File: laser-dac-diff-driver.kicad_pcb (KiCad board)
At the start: 2 copper layers, 53 parts, among them IC401 DCDC-CONV_TRACO_TMH-XXXX_Dual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, P101 CONN_2, P102 CONN_3X2, P103 CONN_6X2, U101 AD5689RARUZ, U102 74HC04, U201 OP470, U202 LM358, U401 LM317EMP, U402 LM317EMP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

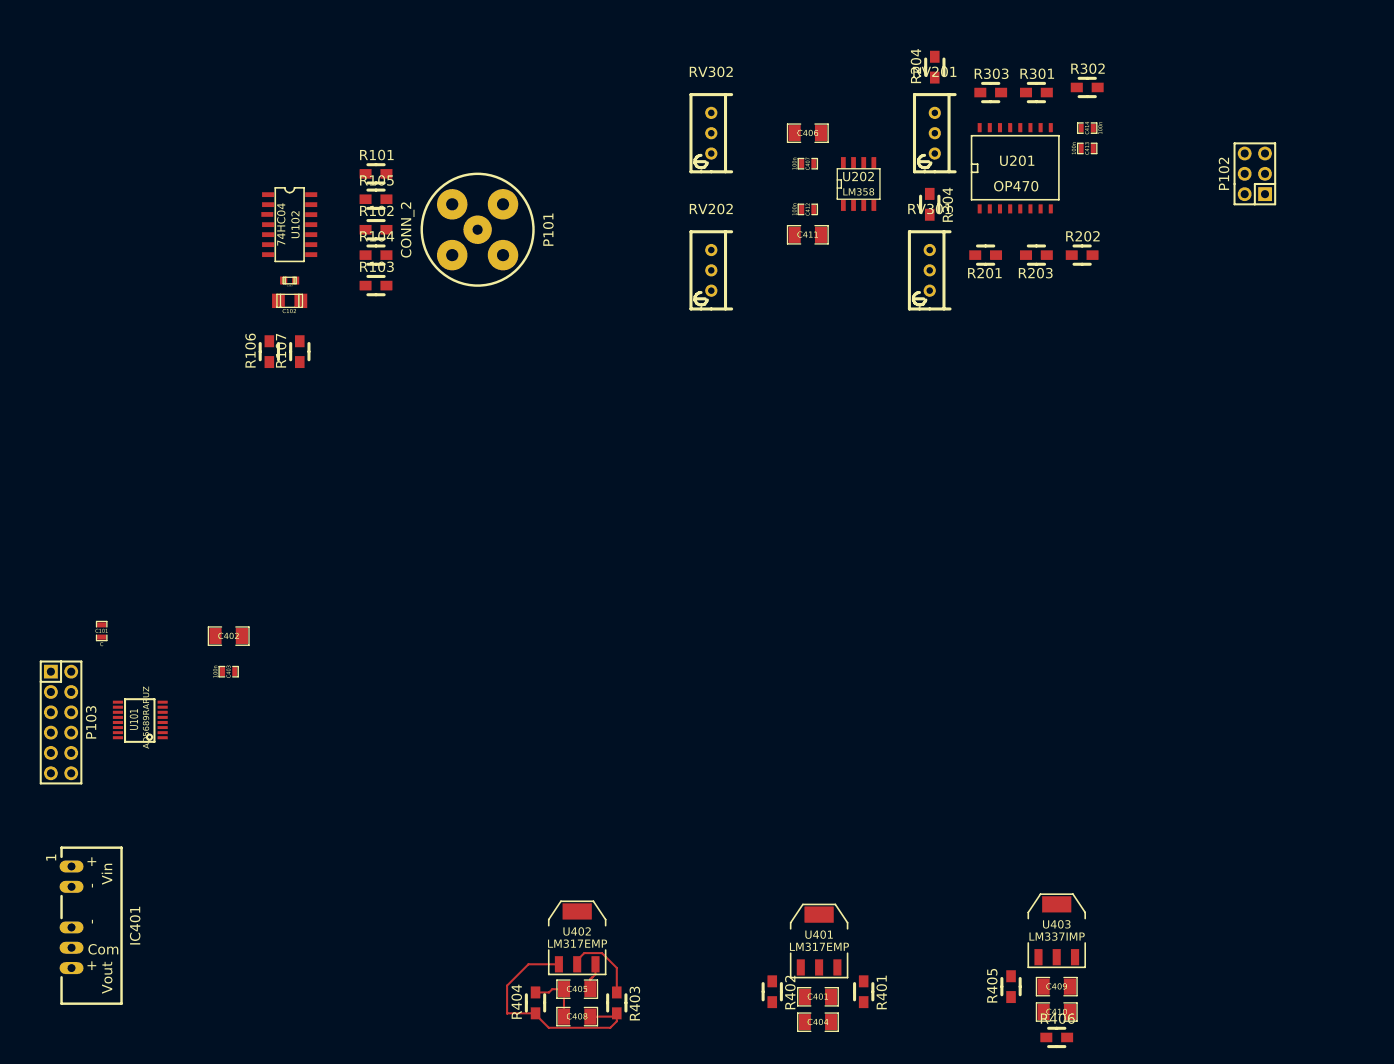
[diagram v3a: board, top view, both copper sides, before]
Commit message: Started layout, final-ish positions
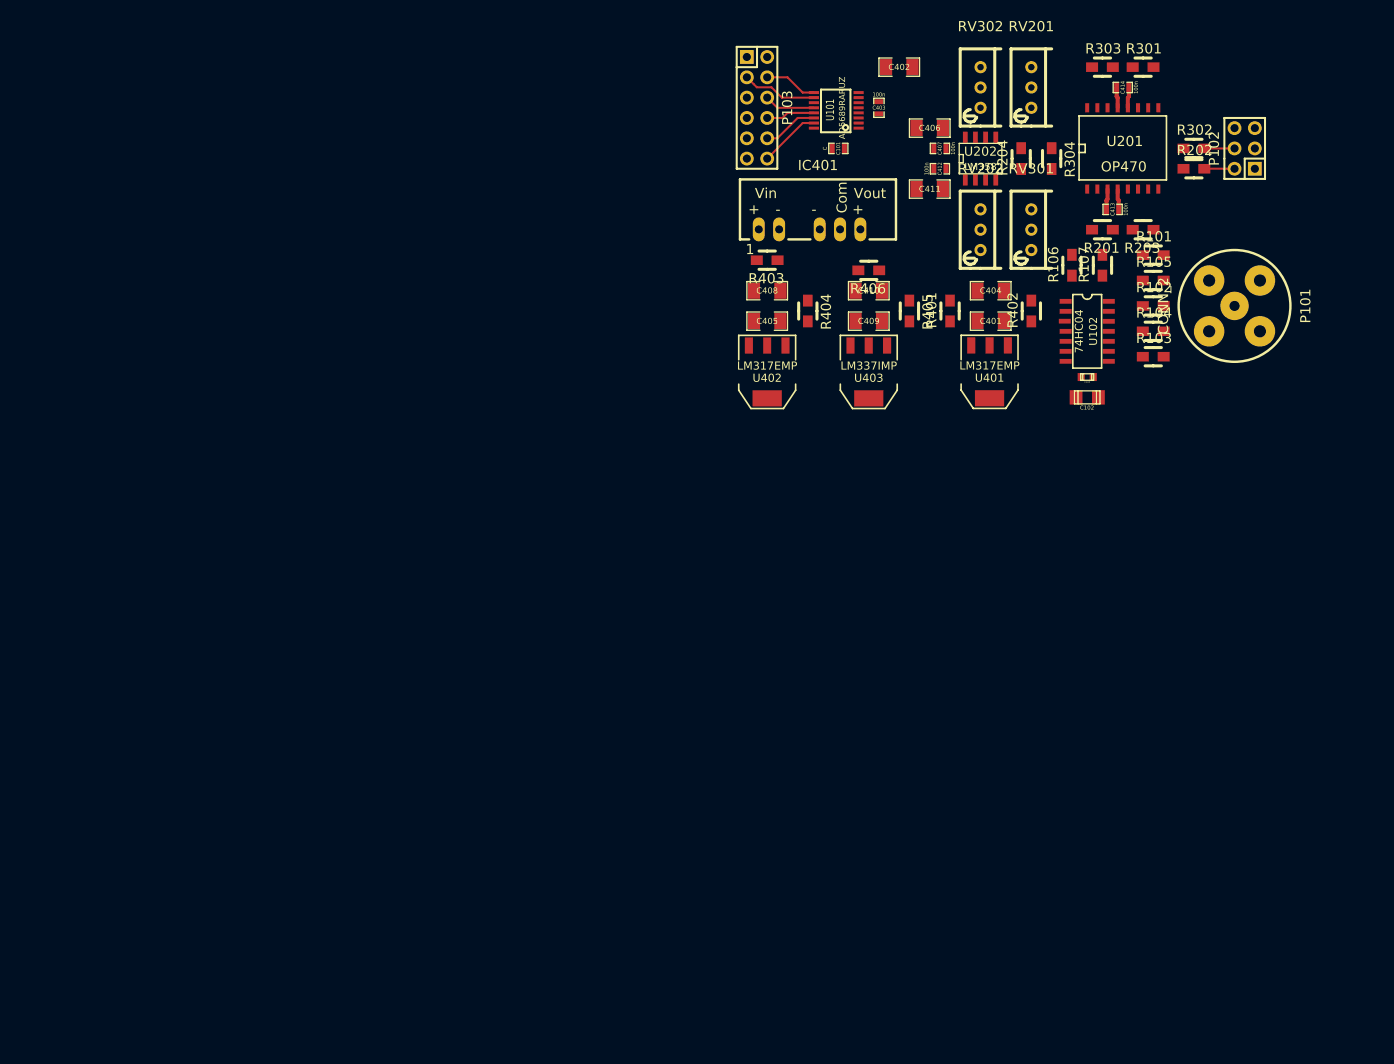
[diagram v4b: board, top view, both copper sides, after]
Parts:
- moved IC401 127.5 mm to (218.4, 44.5), turned to 0 degrees
- moved P103 116.1 mm to (210.8, 31.8)
- moved U101 115.6 mm to (223.5, 34.3)
- moved C101 110.1 mm to (221.0, 36.8), turned to 0 degrees
- moved C402 109.9 mm to (228.6, 26.7)
- moved C403 107.6 mm to (226.1, 31.8), turned to 270 degrees
- moved R107 100.9 mm to (254.0, 51.4)
- moved R106 100.9 mm to (250.2, 51.4)
- moved U102 100.6 mm to (252.1, 59.7)
- moved C103 100.4 mm to (252.1, 65.4)
- moved C102 100.4 mm to (252.1, 67.9)
- moved R406 98.7 mm to (224.8, 52.1), turned to 180 degrees
- moved R101 97.7 mm to (260.4, 50.2)
- moved R105 97.7 mm to (260.4, 53.3)
- moved R102 97.6 mm to (260.4, 56.5)
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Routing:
- net Net-(C408-Pad1): track 30.5 -> 0.00 mm
- net /GAIN: track 0.00 -> 9.43 mm
- net /~RESET: track 0.00 -> 7.68 mm
- net VAA: track 9.67 -> 2.59 mm
- net /SDIN: track 0.00 -> 6.89 mm
- net /~LDAC: track 0.00 -> 6.63 mm
- net /SCLK: track 0.00 -> 6.37 mm
- net /~SYNC: track 0.00 -> 6.11 mm
- net /analog2/Out1+: track 0.00 -> 3.78 mm
- net /analog/Out1+: track 0.00 -> 3.78 mm
- net Net-(C401-Pad1): track 3.41 -> 0.00 mm
- net -VAA: track 0.00 -> 2.59 mm
- net DGND: track 7.16 -> 5.19 mm
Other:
- net class Signal removed
- net class asdf removed

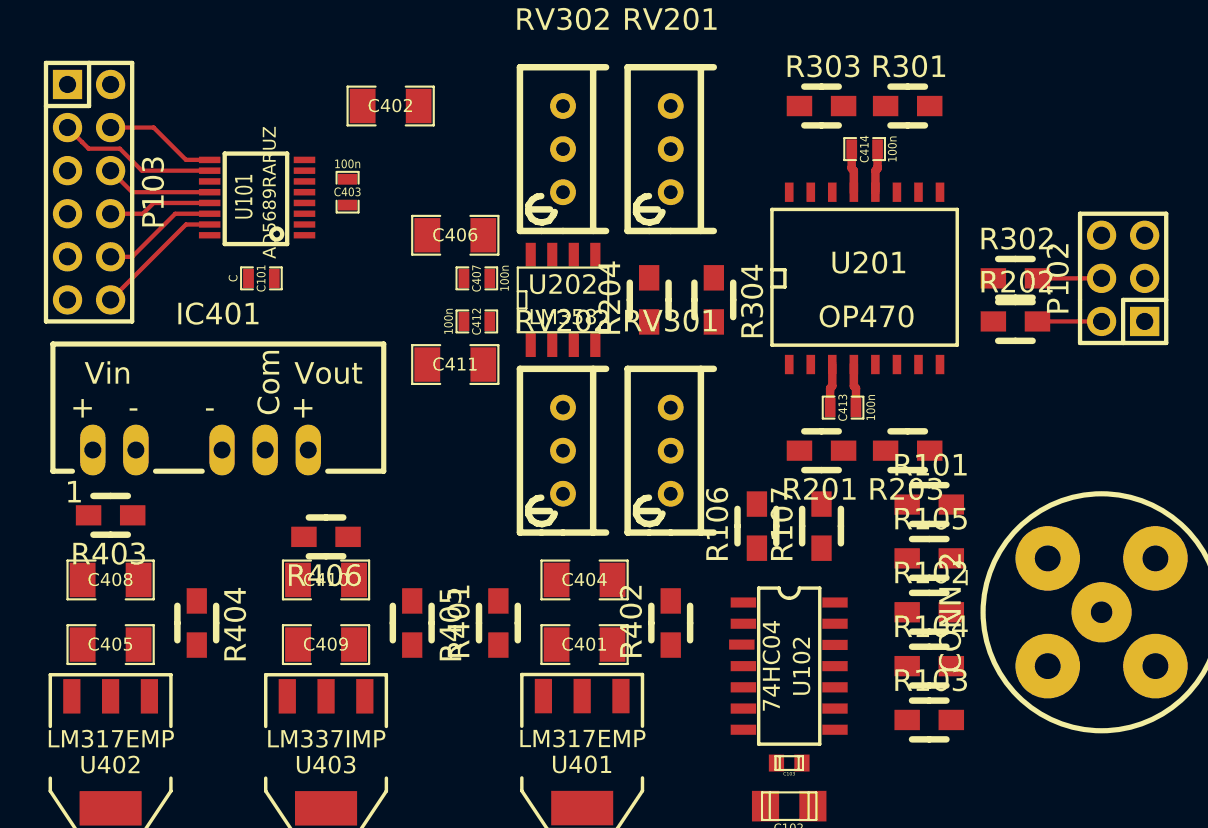
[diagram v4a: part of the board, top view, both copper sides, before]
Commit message: Added net-names for unregulated DCDC outputs, more layout done
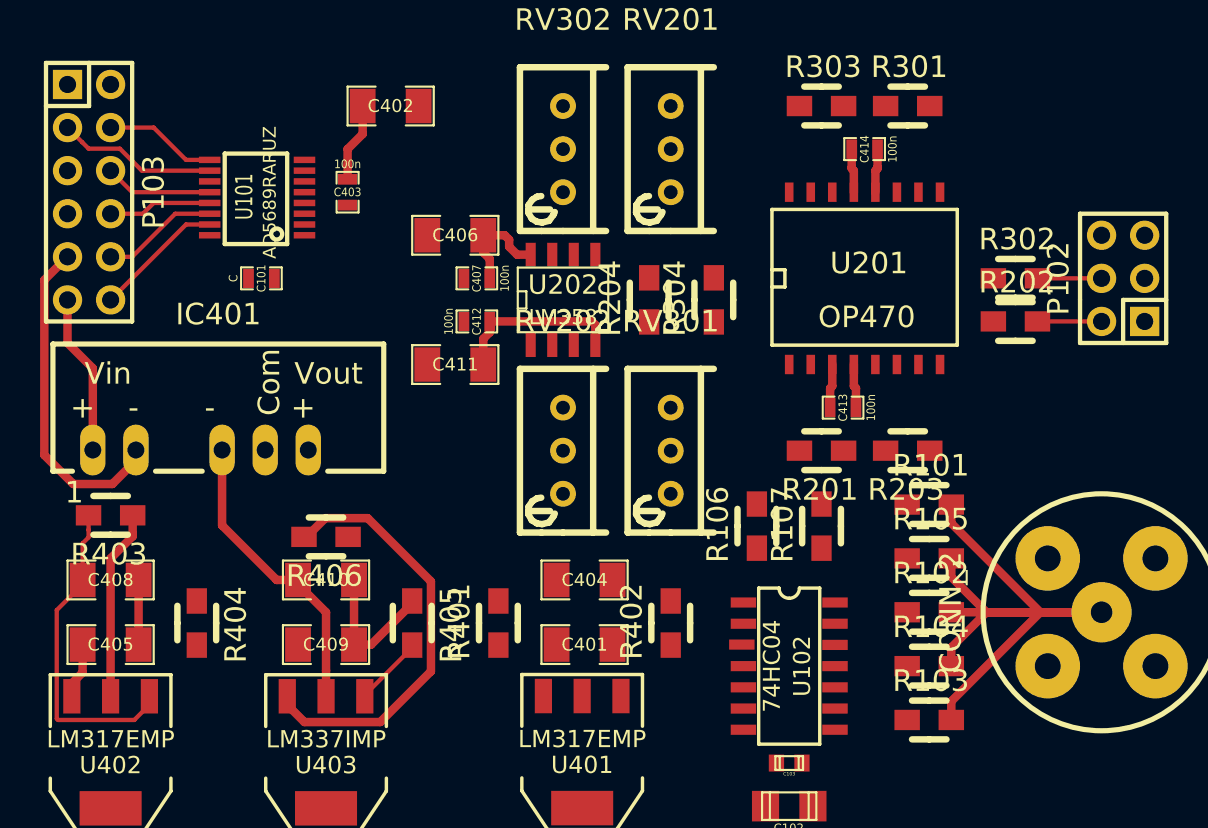
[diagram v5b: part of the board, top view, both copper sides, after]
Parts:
- turned C409 to 180 degrees
- turned R304 to 90 degrees
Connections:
- net Net-(C401-Pad1) renamed /powersupply/+Vout_unreg
- net Net-(C410-Pad2) renamed /powersupply/-Vout_unreg
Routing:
- net /MOD_OUT: track 0.00 -> 47.2 mm
- net -VAA: track 2.59 -> 38.2 mm
- net DGND: track 5.19 -> 36.9 mm
- net Net-(C408-Pad1): track 0.00 -> 19.3 mm
- net /powersupply/-Vout_unreg: track 0.00 -> 17.8 mm
- net VAA: track 2.59 -> 20.0 mm
- net /powersupply/+Vin: track 0.00 -> 9.47 mm
- net +5VD: track 0.00 -> 4.69 mm
- net Net-(C409-Pad2): track 0.00 -> 4.17 mm
- net /powersupply/+Vout_unreg: track 0.00 -> 3.31 mm

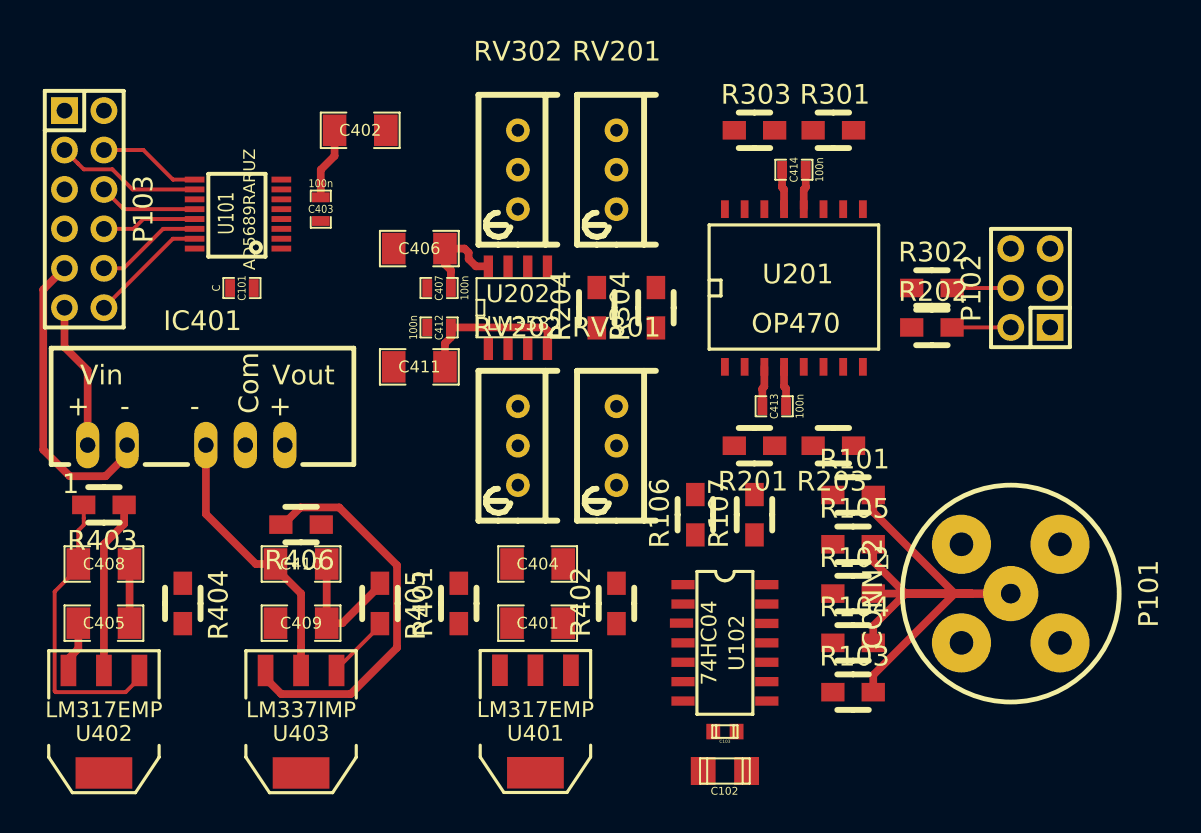
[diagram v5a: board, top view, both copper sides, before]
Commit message: Made SVG schematics, started layout (but it's ugly, need to re-visit positions)
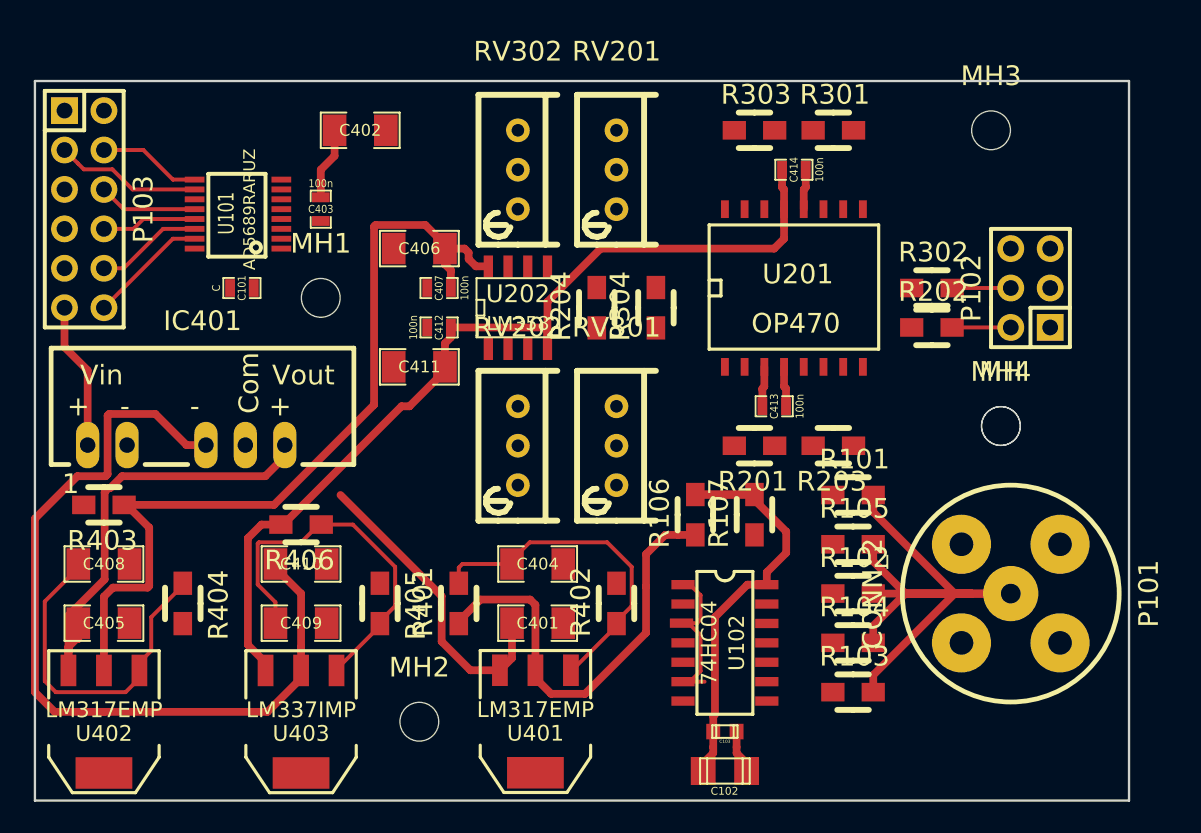
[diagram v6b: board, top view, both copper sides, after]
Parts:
- added MH, MH4: MountingHole_2-5mm_RevA_Date21Jun2010, Mounting_Holes:MountingHole_2-5mm, F.Cu at (269.9, 45.7)
- added MH1: MountingHole_2-5mm_RevA_Date21Jun2010, Mounting_Holes:MountingHole_2-5mm, F.Cu at (226.1, 37.5)
- added MH2: MountingHole_2-5mm_RevA_Date21Jun2010, Mounting_Holes:MountingHole_2-5mm, F.Cu at (232.4, 64.8)
- added MH3: MountingHole_2-5mm_RevA_Date21Jun2010, Mounting_Holes:MountingHole_2-5mm, F.Cu at (269.2, 26.7)
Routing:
- net /powersupply/+Vout_unreg: track 3.31 -> 49.2 mm
- net VAA: track 20.0 -> 58.4 mm
- net /powersupply/-Vout_unreg: track 17.8 -> 54.6 mm
- net /MOD_VCC: track 0.00 -> 29.0 mm
- net DGND: track 36.9 -> 7.99 mm
- net +5VD: track 4.69 -> 33.1 mm
- net -VAA: track 38.2 -> 61.6 mm
- net Net-(C404-Pad1): track 0.00 -> 22.0 mm
- net Net-(C409-Pad2): track 4.17 -> 24.3 mm
- net Net-(U102-Pad1): track 0.00 -> 11.0 mm
- net Net-(C408-Pad1): track 19.3 -> 22.5 mm
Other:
- board outline added: 70.5 x 46.4 mm
